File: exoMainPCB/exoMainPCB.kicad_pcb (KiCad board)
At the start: 4 copper layers, 137.5 x 80 mm, 91 parts, among them J1 Conn_02x06_Odd_Even, J10 Conn_01x03_Pin, J11 USB_A, J12 USB_A, J13 USB_A, J14 Screw_Terminal_01x02, J15 Conn_01x03, J16 Conn_01x02, J2 HDMI_A, J3 USB_A, J4 Conn_01x02, J5 Conn_01x03, J6 Conn_01x03_Pin, J7 Conn_01x02, J8 Screw_Terminal_01x02, J9 Conn_01x12, SW1 SW_SPDT, SW2 SW_Push, SW3 SW_SPDT, U1 MCP2515-I/ST, U14 SI8642ED-B-IS, U15 SN65HVD230D, U17 SM24CANB-02HTG, U2 MCP2515-I/ST, U3 BNO085, U4 SL2.1A, U5 MCP3008, U7 SN65HVD230D, U8 SM24CANB-02HTG, Y1 16 MHz, Y2 16 MHz, Y3 12 MHz, Y4 32.768 kHz

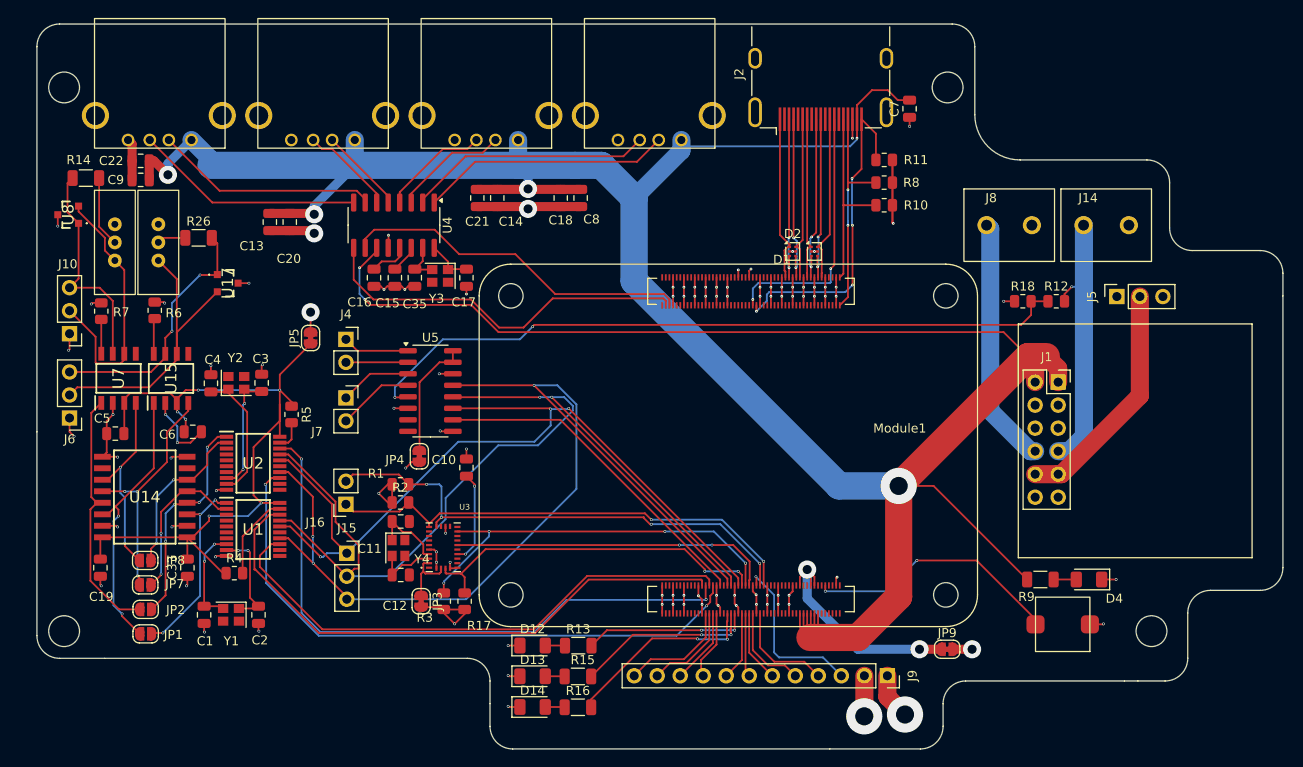
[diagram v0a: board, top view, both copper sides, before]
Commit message: added pours and cleaned up labels
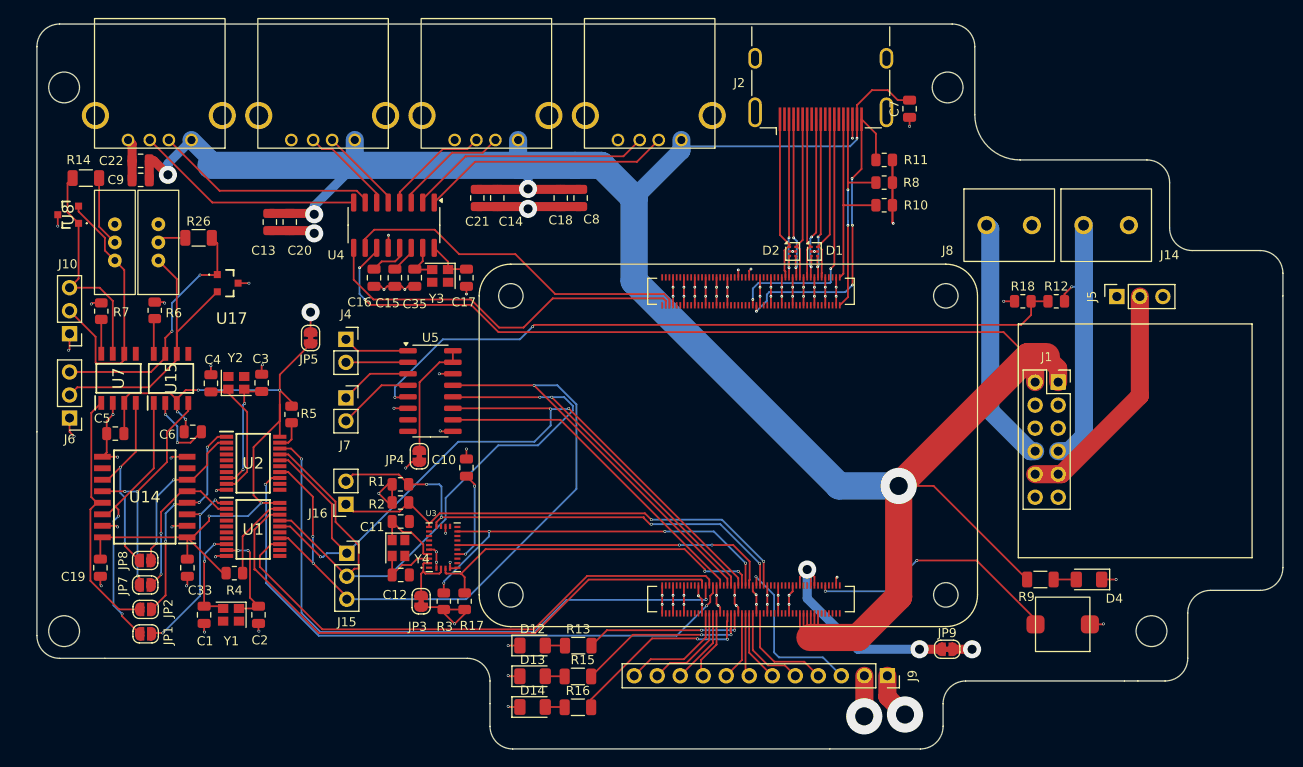
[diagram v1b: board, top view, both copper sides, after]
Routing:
- added copper zone on In1.Cu, net +3V3
- added copper zone on In2.Cu, net GND

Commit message: added silkscreen labels, completed ground pours
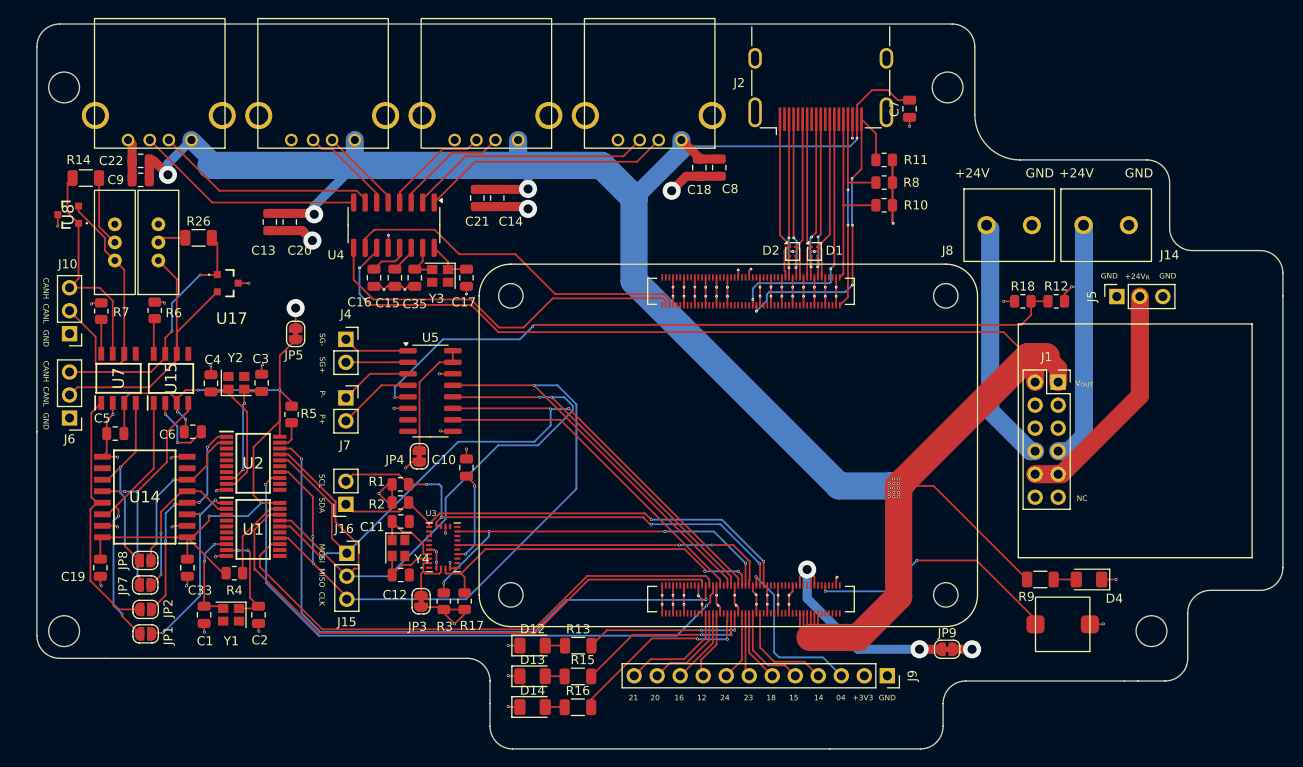
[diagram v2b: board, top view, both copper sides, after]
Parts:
- moved C8 15.7 mm to (137.8, 40.9)
- moved C18 15.7 mm to (135.6, 40.9)
- moved JP5 1.71 mm to (91.0, 59.2)
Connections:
- C19 pad 1: GNDS -> GND
- C33 pad 1: GNDS -> GND
- C5 pad 1: GNDS -> GND
- C6 pad 2: GNDS -> GND
- J10 pad 1: GNDS -> GND
- J6 pad 1: GNDS -> GND
- R6 pad 2: GNDS -> GND
- R7 pad 2: GNDS -> GND
- U14 pad 15: GNDS -> GND
- U14 pad 2: GNDS -> GND
- U14 pad 9: GNDS -> GND
- U15 pad 2: GNDS -> GND
- U17 pad 3: GNDS -> GND
- U7 pad 2: GNDS -> GND
- U8 pad 3: GNDS -> GND
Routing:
- net GND: track 238.0 -> 167.2 mm, vias 83 -> 95
- net GNDS: track 30.7 -> 0.00 mm, vias 14 -> 0
- net +3.3V: track 4.48 -> 0.00 mm, vias 1 -> 0
- net +5V: track 353.3 -> 352.6 mm, vias 7 -> 20
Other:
- board text added: "+24V"
- board text added: "+24V_{R}"
- board text added: "+3V3"
- board text added: "04"
- board text added: "12"
- board text added: "14"
- board text added: "15"
- board text added: "16"
- board text added: "18"
- board text added: "20"
- board text added: "21"
- board text added: "23"
- board text added: "24"
- board text added: "CANH"
- board text added: "CANL"
- board text added: "CLK"
- board text added: "GND"
- board text added: "MISO"
- board text added: "MOSI"
- board text added: "NC"
- board text added: "P+"
- board text added: "P-"
- board text added: "SCL"
- board text added: "SDA"
- board text added: "SG+"
- board text added: "SG-"
- board text added: "V_{OUT}"

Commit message: modified via size to match IO board, resolved all errors
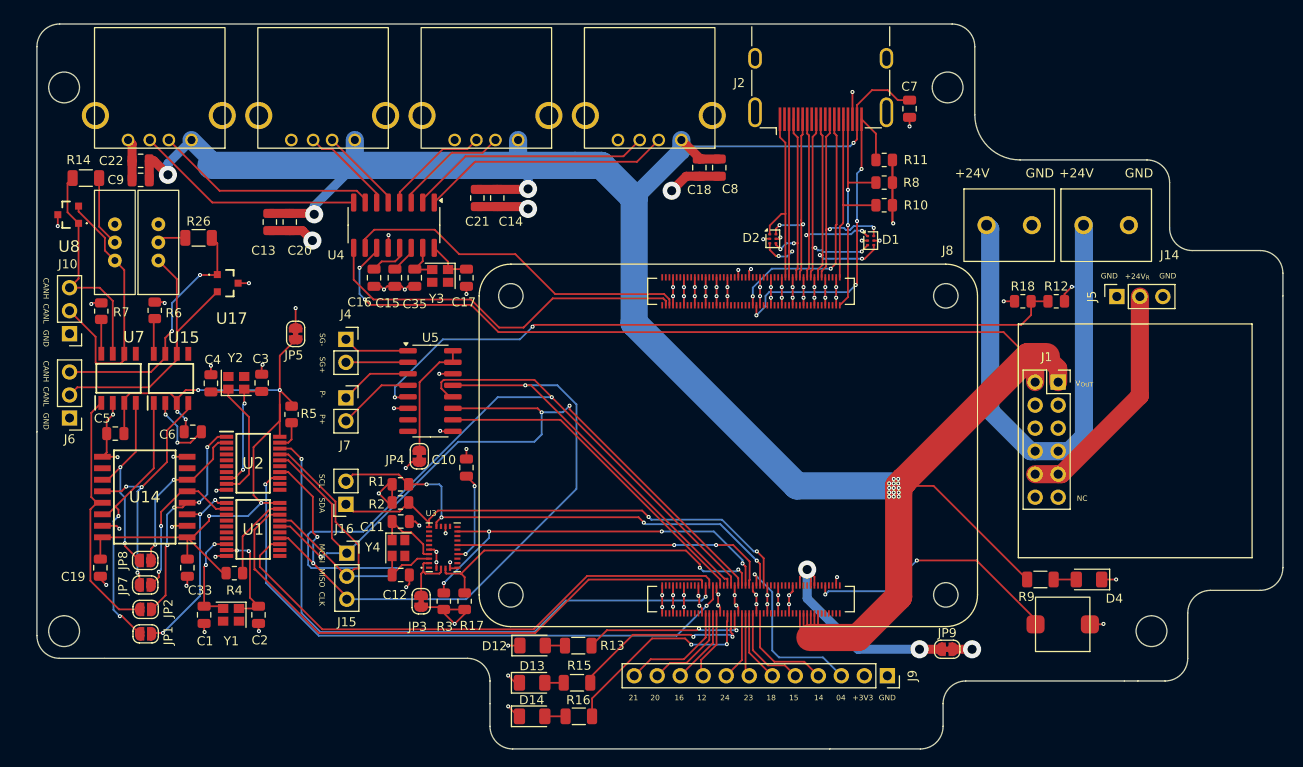
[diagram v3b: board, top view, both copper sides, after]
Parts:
- moved D1 6.32 mm to (154.5, 48.9)
- moved D2 2.60 mm to (143.7, 48.7)
- moved D14 1.03 mm to (117.2, 101.4)
- moved R16 1.00 mm to (122.3, 101.4)
- moved D13 0.72 mm to (117.2, 97.7)
- moved R15 0.71 mm to (122.1, 97.7)
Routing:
- net GND: track 167.2 -> 189.2 mm, vias 95 -> 99
- net /MISO: track 105.4 -> 125.1 mm, vias 2 -> 1
- net /D_{HDMI0_TX0_P}: track 17.9 -> 25.1 mm, vias 0 -> 2
- net /D_{HDMI0_CLK_P}: track 18.9 -> 25.2 mm
- net /D_{HDMI0_CLK_N}: track 18.3 -> 24.4 mm, vias 0 -> 2
- net /D_{HDMI0_TX0_N}: track 19.0 -> 24.3 mm
- net /D_{HDMI0_TX1_N}: track 18.1 -> 21.6 mm, vias 0 -> 2
- net /D_{HDMI0_TX2_N}: track 18.8 -> 21.5 mm
- net /D_{HDMI0_TX2_P}: track 18.3 -> 20.9 mm
- net +24V: track 57.6 -> 60.1 mm
- net /D_{HDMI0_TX1_P}: track 19.1 -> 20.7 mm
- net /STATUS_{3}: track 21.7 -> 23.3 mm
- net /STATUS_{2}: track 19.7 -> 21.2 mm
- net +5V: track 352.6 -> 354.1 mm
- net /RXD_0B: track 26.4 -> 27.8 mm
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
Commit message: added e stop screw terminal, corrected vias, traces, and pours
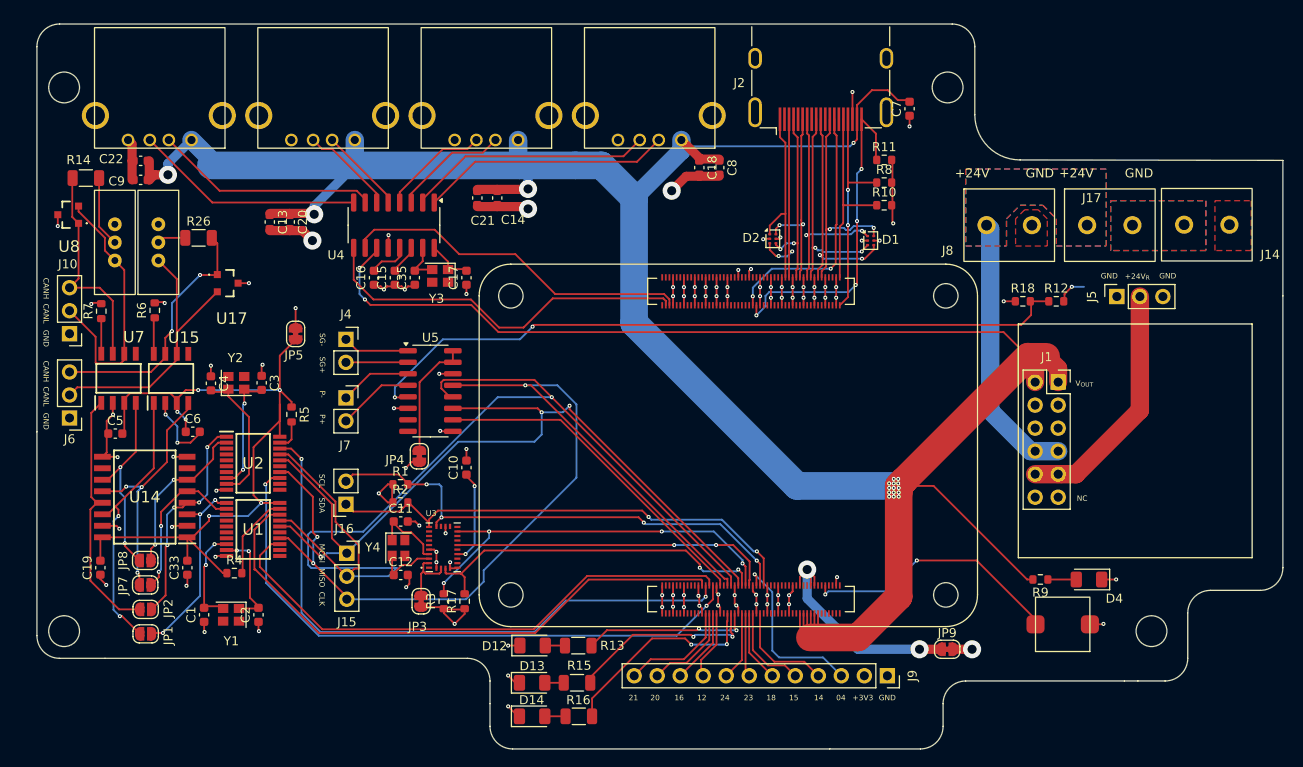
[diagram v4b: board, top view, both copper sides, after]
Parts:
- added J17: Screw_Terminal_01x02, BNO085:1x2 Screw Terminal C3703, F.Cu at (180.9, 47.2)
- C1, C10, C11, C12, C13, C14, C15, C16, C17, C18, C19, C2, C20, C21, C22, C3, C33, C35, C4, C5, C6, C7, C8, C9: footprint Capacitor_SMD:C_0805_2012Metric -> Capacitor_SMD:C_0603_1608Metric
- R1, R10, R11, R12, R17, R18, R2, R3, R4, R5, R6, R7, R8: footprint Resistor_SMD:R_0805_2012Metric -> Resistor_SMD:R_0603_1608Metric
- R9: footprint Resistor_SMD:R_1206_3216Metric -> Resistor_SMD:R_0603_1608Metric
- moved J14 11.1 mm to (191.6, 47.1)
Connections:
- J14 pad 1: +24V -> /V_{mot}
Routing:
- net +24V: track 60.1 -> 33.3 mm
- net GND: track 189.2 -> 172.9 mm
- net /V_{RP}: track 26.1 -> 27.0 mm
- net Net-(D4-A): track 2.50 -> 3.14 mm
- added copper zone on In2.Cu, net (none)
- added copper zone on B.Cu, net +24V
- added copper zone on F.Cu, net +24V
- added copper zone on In1.Cu, net +24V
- added copper zone on In2.Cu, net +24V
- added copper zone on B.Cu, net /V_{mot}
- added copper zone on F.Cu, net /V_{mot}
- added copper zone on In1.Cu, net /V_{mot}
- added copper zone on In2.Cu, net /V_{mot}
- added copper zone on F.Cu, net GND
- added copper zone on In1.Cu, net GND
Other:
- outline, holes or cut-outs redrawn

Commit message: FIXED condensed pcb layout, put stuff in the back, replaced headers with GH JST and power terminals with XT60
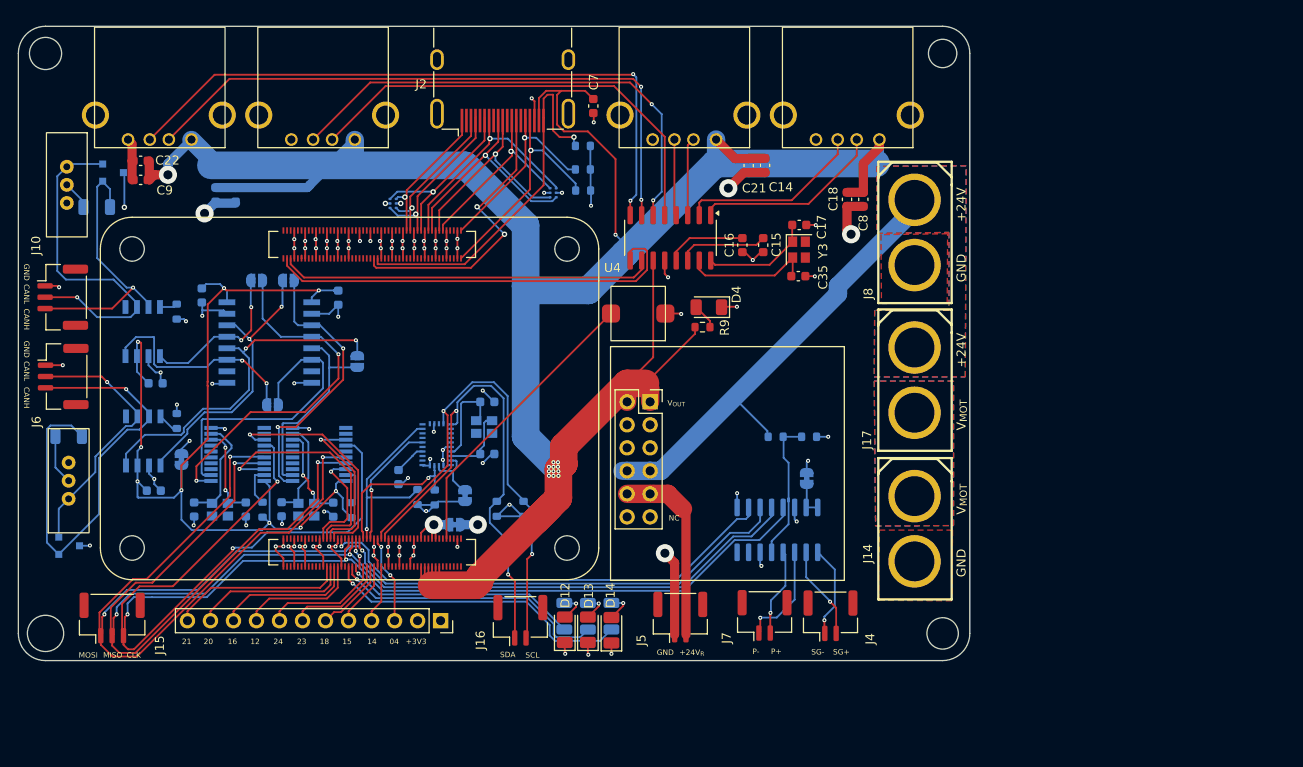
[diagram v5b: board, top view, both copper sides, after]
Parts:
- C1, C3, C4: value 22 pF -> 22pF; moved to B.Cu
- C10: value 0.1 uF -> 0.1uF; moved to B.Cu
- C11, C12, C13, C19, C2, C20, C33, C5, C6, D1, D2, JP1, JP2, JP3, JP4, JP5, JP7, JP8, JP9, R1, R10, R11, R12, R13, R14, R15, R16, R17, R18, R2, R26, R3, R4, R5, R6, R7, R8, U1, U14, U15, U17, U2, U3, U5, U7, U8, Y1, Y2, Y4: moved to B.Cu
- C15, C16: value 10 uF -> 10uF
- J10, J6: footprint Connector_PinHeader_2.54mm:PinHeader_1x03_P2.54mm_Vertical -> Connector_JST:JST_GH_BM03B-GHS-TBT_1x03-1MP_P1.25mm_Vertical
- J14, J17, J8: footprint BNO085:1x2 Screw Terminal C3703 -> XT60:CONN-TH_XT60
- J15: footprint Connector_PinSocket_2.54mm:PinSocket_1x03_P2.54mm_Vertical -> Connector_JST:JST_GH_BM03B-GHS-TBT_1x03-1MP_P1.25mm_Vertical
- J16, J4, J7: footprint Connector_PinSocket_2.54mm:PinSocket_1x02_P2.54mm_Vertical -> Connector_JST:JST_GH_BM02B-GHS-TBT_1x02-1MP_P1.25mm_Vertical
- J5: footprint Connector_PinSocket_2.54mm:PinSocket_1x03_P2.54mm_Vertical -> Connector_JST:JST_GH_BM02B-GHS-TBT_1x02-1MP_P1.25mm_Vertical
- moved J4 61.6 mm to (150.1, 90.3)
- moved J5 59.8 mm to (133.5, 90.5), turned to 0 degrees
- moved SW2 58.1 mm to (127.3, 53.5)
- moved JP9 56.1 mm to (108.6, 80.2)
- moved J7 52.1 mm to (142.8, 90.3)
- moved D4 51.6 mm to (136.7, 56.2)
- moved J9 49.7 mm to (107.0, 90.8)
- moved R9 46.5 mm to (135.9, 58.5)
- moved J14 46.5 mm to (159.3, 80.7), turned to -90 degrees
- moved J1 45.1 mm to (130.2, 66.7)
- moved JP4 42.8 mm to (147.4, 75.2), turned to 90 degrees
- moved C35 42.3 mm to (146.5, 52.8), turned to 180 degrees
- moved Module1 42.1 mm to (121.0, 82.8)
- moved D2 42.1 mm to (101.8, 44.8), turned to 180 degrees
- moved JP1 42.1 mm to (90.2, 53.3)
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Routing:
- net +5V: track 354.3 -> 273.7 mm, vias 20 -> 13
- net /MOSI: track 93.1 -> 157.2 mm, vias 3 -> 4
- net /V_{battery}: track 79.5 -> 16.5 mm, vias 2 -> 0
- net /SCK: track 109.0 -> 160.7 mm, vias 3 -> 4
- net /D_{CS0}: track 63.2 -> 11.9 mm, vias 0 -> 1
- net Net-(J13-D+): track 25.4 -> 72.3 mm, vias 0 -> 2
- net Net-(J13-D-): track 24.7 -> 69.5 mm, vias 0 -> 2
- net Net-(J12-D+): track 10.5 -> 54.4 mm, vias 0 -> 2
- net /D_{INT1}: track 67.7 -> 25.3 mm, vias 2 -> 1
- net /D_{INT0}: track 59.7 -> 17.6 mm, vias 0 -> 1
- net /D_{CS1}: track 68.2 -> 26.3 mm, vias 2 -> 1
- net Net-(J12-D-): track 9.46 -> 50.1 mm
- net /MISO: track 125.1 -> 153.1 mm, vias 1 -> 4
- net /+3V3_{CAN}: track 84.9 -> 110.2 mm, vias 6 -> 9
- net Net-(J6-Pin_3): track 28.2 -> 52.0 mm, vias 2 -> 1
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- removed copper zone on In2.Cu, net (none)
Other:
- board size 137.5 x 80 mm -> 105 x 70 mm
- board text added: "V_{MOT}"
